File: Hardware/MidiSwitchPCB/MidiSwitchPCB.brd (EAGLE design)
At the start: 160 x 100 mm, 65 parts, among them IC1 74AHC1G04DBV, IC2 74AHC1G04DBV, K1 APF30212C, K2 APF30212C, K3 APF30212C, K4 APF30212C, K5 APF30212C, K6 APF30212C, K7 APF30212C, K8 APF30212C, Q1 BSS123, Q2 BSS123, Q3 BSS123, Q4 BSS123, Q5 BSS123, Q6 BSS123, Q7 BSS123, Q8 BSS123, X1 1503_09, X2 1503_09, X3 1503_09, X4 1503_09

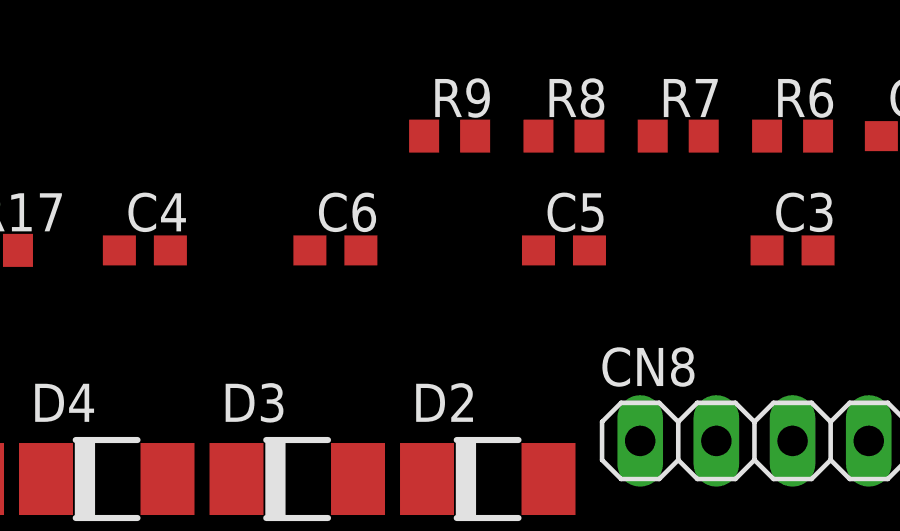
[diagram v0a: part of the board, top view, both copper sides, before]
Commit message: added switching capacitor to part list (changed cap-package in layout from 0603 to 1206)
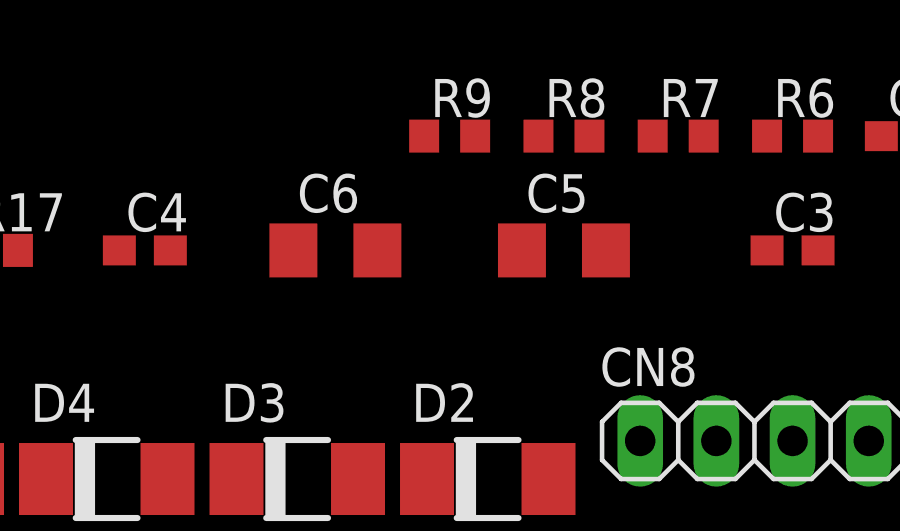
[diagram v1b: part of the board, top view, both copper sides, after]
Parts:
- C5, C6: device rcl:C0603 -> rcl:C1206
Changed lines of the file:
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@@
 <setting verticaltext="up"/>
 </settings>
-<grid distance="0.05" unitdist="inch" unit="inch" style="lines" multiple="1" display="no" altdistance="0.025" altunitdist="inch" altunit="inch"/>
+<grid distance="0.1" unitdist="mm" unit="mm" style="lines" multiple="1" display="yes" altdistance="0.025" altunitdist="inch" altunit="mm"/>
 <layers>
 <layer number="1" name="Top" color="4" fill="1" visible="yes" active="yes"/>
@@
 <element name="C3" library="rcl" package="C0603" value="100nF" x="-44.45" y="106.68"/>
 <element name="C4" library="rcl" package="C0603" value="22µF" x="-66.04" y="106.68"/>
-<element name="C5" library="rcl" package="C0603" value="100nF" x="-52.07" y="106.68"/>
-<element name="C6" library="rcl" package="C0603" value="100nF" x="-59.69" y="106.68"/>
+<element name="C5" library="rcl" package="C1206" value="100nF" x="-52.07" y="106.68"/>
+<element name="C6" library="rcl" package="C1206" value="100nF" x="-59.69" y="106.68"/>
 <element name="L1" library="rcl" package="POWER-CHOKE_WE-TPC" value="4.7µH" x="-80.01" y="35.56"/>
 <element name="C7" library="rcl" package="C0603" value="10µF 40V" x="-27.94" y="106.68"/>
@@
 <contactref element="C5" pad="1"/>
 <contactref element="L1" pad="2"/>
-<wire x1="-52.92" y1="106.68" x2="-19.922" y2="96.905" width="0" layer="19" extent="1-1"/>
-<wire x1="-80.01" y1="33.51" x2="-52.92" y2="106.68" width="0" layer="19" extent="1-1"/>
+<wire x1="-53.47" y1="106.68" x2="-19.922" y2="96.905" width="0" layer="19" extent="1-1"/>
+<wire x1="-80.01" y1="33.51" x2="-53.47" y2="106.68" width="0" layer="19" extent="1-1"/>
 </signal>
 <signal name="N$54">
 <contactref element="PS1" pad="19"/>
 <contactref element="C5" pad="2"/>
-<wire x1="-51.22" y1="106.68" x2="-19.922" y2="96.255" width="0" layer="19" extent="1-1"/>
+<wire x1="-50.67" y1="106.68" x2="-19.922" y2="96.255" width="0" layer="19" extent="1-1"/>
 </signal>
 <signal name="N$55">
@@
 <contactref element="PS1" pad="2"/>
 <contactref element="C6" pad="1"/>
-<wire x1="-60.54" y1="106.68" x2="-25.798" y2="96.255" width="0" layer="19" extent="1-1"/>
-<wire x1="-80.01" y1="37.61" x2="-60.54" y2="106.68" width="0" layer="19" extent="1-1"/>
+<wire x1="-61.09" y1="106.68" x2="-25.798" y2="96.255" width="0" layer="19" extent="1-1"/>
+<wire x1="-80.01" y1="37.61" x2="-61.09" y2="106.68" width="0" layer="19" extent="1-1"/>
 </signal>
 <signal name="N$56">
 <contactref element="C6" pad="2"/>
 <contactref element="PS1" pad="3"/>
-<wire x1="-58.84" y1="106.68" x2="-25.798" y2="95.605" width="0" layer="19" extent="1-1"/>
+<wire x1="-58.29" y1="106.68" x2="-25.798" y2="95.605" width="0" layer="19" extent="1-1"/>
 </signal>
 <signal name="N$53">

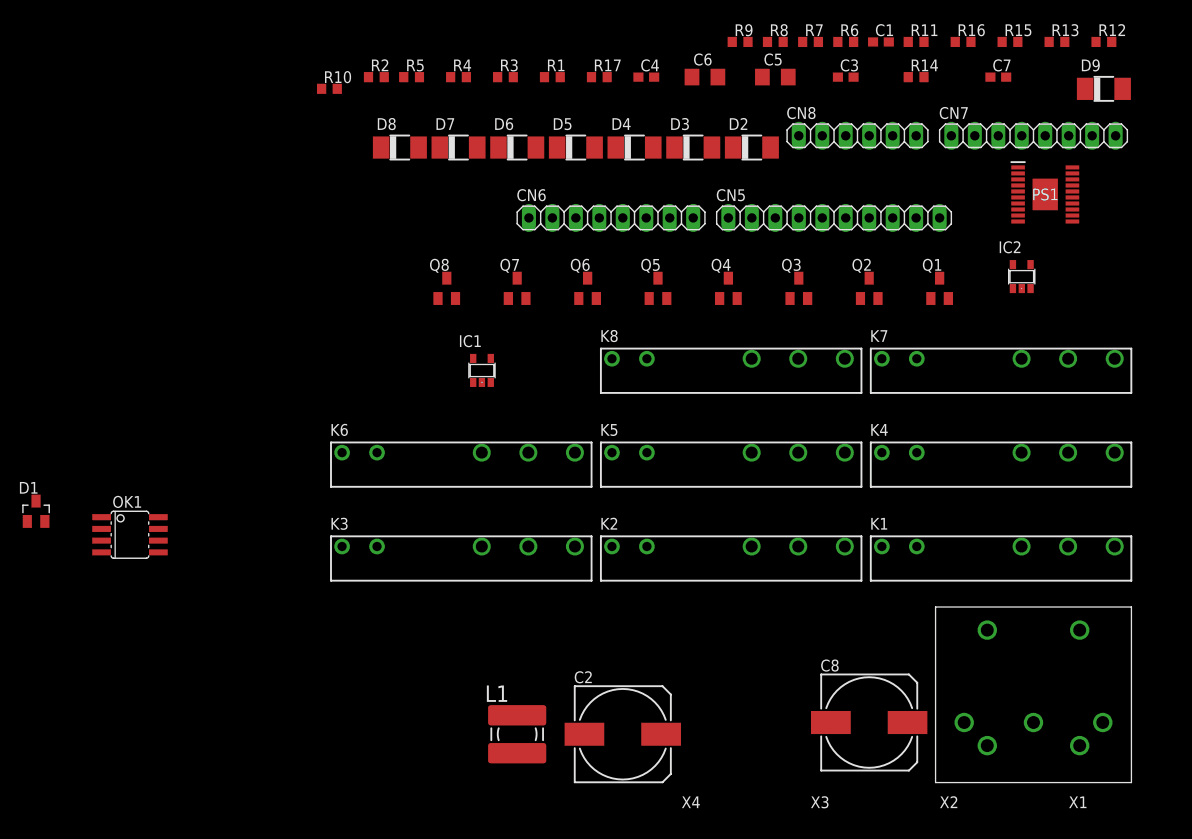
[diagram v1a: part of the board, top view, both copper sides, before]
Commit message: added some part libraries
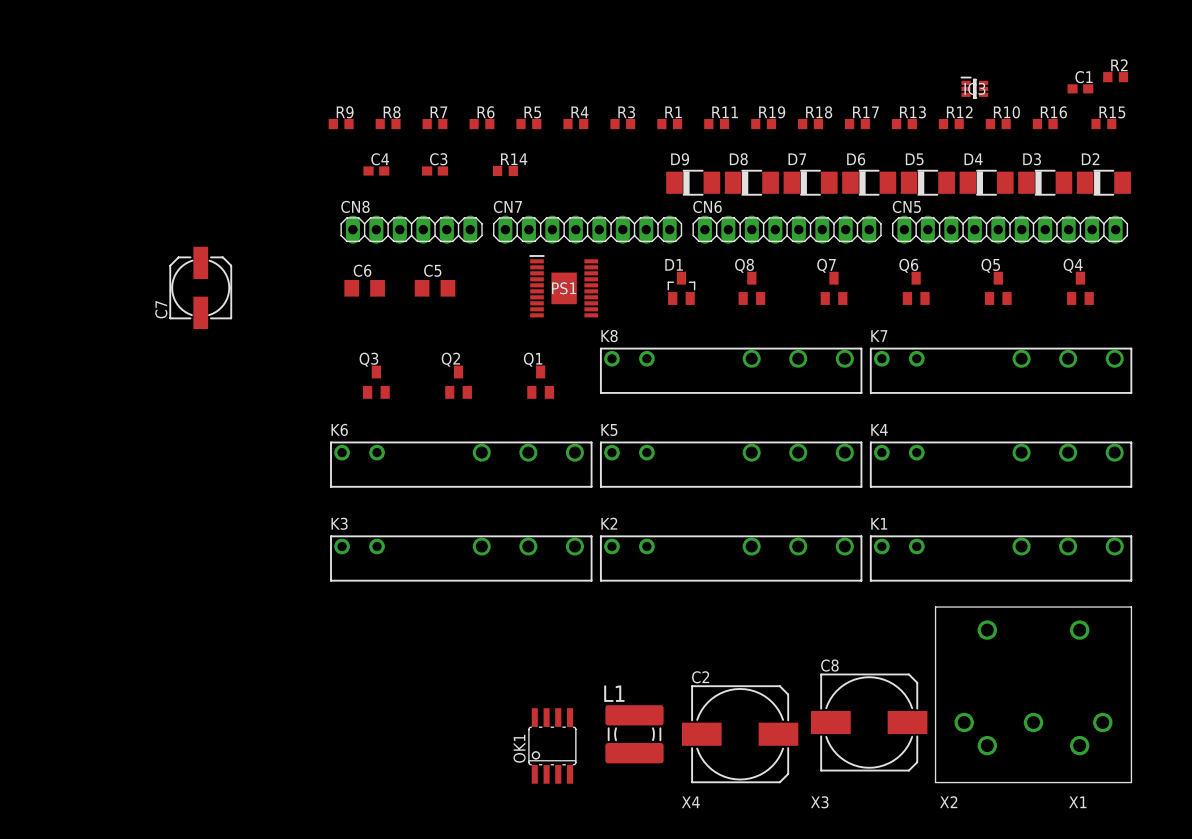
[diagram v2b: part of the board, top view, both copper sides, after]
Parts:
- removed IC1, IC2: 74AHC1G04DBV, 74xx-little-de:SOT23-5
- added IC3: 74LVC2G04GW,125, 74LVC2G04GW_125:SOT65P210X110-6N
- added R18, R19: 0R, rcl:R0603
- C7: device rcl:C0603 -> rcl:153CLV-0605
- moved C7 89.3 mm to (-114.3, 83.9), turned to 90 degrees
- moved R2 80.0 mm to (-15.2, 106.7)
- moved D1 73.9 mm to (-62.2, 83.8)
- moved R10 72.5 mm to (-27.9, 101.6)
- moved PS1 53.1 mm to (-74.9, 83.8)
- moved OK1 51.1 mm to (-76.2, 34.3), turned to 0 degrees
- moved CN7 49.3 mm to (-72.4, 90.2)
- moved CN8 49.3 mm to (-91.4, 90.2)
- moved Q3 46.8 mm to (-95.2, 73.7)
- moved C3 45.6 mm to (-88.9, 96.5)
- moved D9 45.6 mm to (-61.0, 95.2)
- moved Q2 45.6 mm to (-86.4, 73.7)
- moved R14 45.6 mm to (-81.3, 96.5)
- moved Q1 44.4 mm to (-77.5, 73.7)
- moved R9 44.1 mm to (-99.1, 101.6)
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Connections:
- new net N$58: PS1.8, R18.2, R19.1
- new net VCC_3_3: IC3.5, OK1.8, R3.2, R5.2
- new net VCC_6-8: C1.1, C2.+, C3.1, C4.1, CN6.8, D2.C, D3.C, D4.C, D5.C, D6.C, D7.C, D8.C, D9.C, K1.1, K2.1, K3.1, K4.1, K5.1, K6.1, K7.1, K8.1, PS1.16, PS1.17, R14.1, R15.2
- net GND: now also C7.-, IC3.2, R19.2; no longer C7.2, IC1.3, IC2.3
- net MIDI_RX: now also IC3.3; no longer IC1.2
- net N$1: now also IC3.1, IC3.4; no longer IC1.4, IC2.2
- net N$11: now also IC3.6; no longer IC2.4
- net N$53: now also C7.+, R18.1; no longer C7.1
- net VCC: now also CN6.4; no longer C1.1, C2.+, C3.1, C4.1, CN6.8, D2.C, D3.C, D4.C, D5.C, D6.C, D7.C, D8.C, D9.C, IC1.5, IC2.5, K1.1, K2.1, K3.1, K4.1, K5.1, K6.1, K7.1, K8.1, OK1.8, PS1.16, PS1.17, R14.1, R15.2, R3.2, R5.2

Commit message: continued searching parts
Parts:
- added R20, R21, R22, R23, R24, R25, R26, R27: (no value), rcl:R0603
- C4: device rcl:C0603 -> rcl:C1206
- C8: device rcl:153CLV-1012 -> rcl:C0805
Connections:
- new net N$59: K1.1, R20.1
- new net N$60: K2.1, R22.1
- new net N$61: K3.1, R21.1
- new net N$62: K4.1, R23.1
- new net N$63: K5.1, R24.1
- new net N$64: K6.1, R25.1
- new net N$65: K7.1, R26.1
- new net N$66: K8.1, R27.1
- net GND: now also C8.2; no longer C8.-
- net N$57: now also C8.1; no longer C8.+
- net VCC_6-8: now also R20.2, R21.2, R22.2, R23.2, R24.2, R25.2, R26.2, R27.2; no longer K1.1, K2.1, K3.1, K4.1, K5.1, K6.1, K7.1, K8.1

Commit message: changed some device packages
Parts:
- removed K1: APF30212C, relay:APF30212C
- added J1: 694108106102, SamacSys_Parts:694108106102
- added U$3: G6L-1F-TR_DC5-NEW, SamacSys_Parts:G6L1FTRDC5
- moved U$1 221.4 mm to (127.0, 86.0)
- moved CN8 214.6 mm to (122.2, 70.0)
- moved CN7 203.8 mm to (119.7, 22.0)
- moved OK1 190.6 mm to (113.8, 49.3)
- moved C7 181.0 mm to (55.7, 21.9)
- moved PS1 169.3 mm to (89.1, 41.8)
- moved CN6 154.1 mm to (102.0, 70.0)
- moved R20 143.6 mm to (16.9, 46.7)
- moved R21 143.6 mm to (16.9, 43.3)
- moved R22 143.6 mm to (16.9, 40.0)
- moved R23 143.6 mm to (16.9, 36.6)
- moved R24 143.6 mm to (16.9, 33.3)
- moved R25 143.6 mm to (16.9, 29.9)
- moved R26 143.6 mm to (16.9, 26.6)
- moved R27 143.6 mm to (16.9, 23.2)
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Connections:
- removed net N$53: C7.+, PS1.4, PS1.5, PS1.6, R18.1
- new net N$67: C7.+, J1.1, PS1.4, PS1.5, PS1.6, R18.1
- net GND: now also J1.3
- net N$12: now also U$3.8; no longer K1.2
- net N$36: now also U$3.4; no longer K1.NO
- net N$38: now also U$3.2; no longer K1.COM, K1.NC
- net N$59: now also U$3.5; no longer K1.1

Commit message: placed devices on the layout
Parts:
- removed C3: 100nF, rcl:C0603
- removed C4: 22µF, rcl:C1206
- removed C5, C6: 100nF, rcl:C1206
- removed C7: 10µF 40V, rcl:153CLV-0605
- removed C8: 4.7 µF, rcl:C0805
- removed K2, K3, K4, K5, K6, K7, K8: APF30212C, relay:APF30212C
- removed R14: 10-100k, rcl:R0603
- removed R17, R18, R19: 0R, rcl:R0603
- added C_BST1, C_BST2: 100nF, rcl:C1206
- added C_IN: 10µF 40V, rcl:153CLV-0605
- added C_OUT: 22µF, rcl:C1206
- added C_REG: 4.7 µF, rcl:C0805
- added C_SENS: 100nF, rcl:C0603
- added R_DLY, R_PWRL_DOWN, R_PWRL_UP: 0R, rcl:R0603
- added R_PG: 10-100k, rcl:R0603
- added U$10, U$4, U$5, U$6, U$7, U$8, U$9: G6L-1F-TR_DC5-NEW, SamacSys_Parts:G6L1FTRDC5
- L1: device rcl:POWER-CHOKE_WE-TPC -> NRS8030T4R7MJGJ:NRS8030T4R7MJGJ
- moved R4 202.8 mm to (122.4, 49.9), turned to 90 degrees
- moved R5 202.1 mm to (116.0, 47.8), turned to 180 degrees
- moved R3 199.7 mm to (122.0, 42.0), turned to 90 degrees
- moved R1 190.9 mm to (113.7, 30.7)
- moved D1 187.6 mm to (117.7, 30.8), turned to 90 degrees
- moved C1 175.1 mm to (140.2, 32.4)
- moved R6 173.4 mm to (85.0, 62.0), turned to 180 degrees
- moved R8 168.4 mm to (64.0, 43.1), turned to 180 degrees
- moved R16 166.1 mm to (135.4, 51.0), turned to 90 degrees
- moved R15 163.0 mm to (139.1, 53.1)
- moved IC3 159.9 mm to (119.5, 50.0), turned to 270 degrees
- moved Q1 158.9 mm to (81.0, 63.0), turned to 90 degrees
- moved Q3 158.0 mm to (59.9, 44.0), turned to 90 degrees
- moved R7 157.9 mm to (64.0, 62.0), turned to 180 degrees
- moved R9 147.4 mm to (43.0, 62.1), turned to 180 degrees
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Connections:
- removed net N$50: R15.1
- removed net N$66: K8.1, R27.1
- new net N$53: R23.1, U$6.5
- net GND: now also C_IN.-, C_OUT.2, C_REG.2, C_SENS.2, R_DLY.2, R_PWRL_DOWN.2; no longer C3.2, C4.2, C7.-, C8.2, R17.2, R19.2
- net N$13: now also U$5.8; no longer K3.2
- net N$16: now also U$6.8; no longer K4.2
- net N$19: now also U$5.4; no longer K3.NO
- net N$20: now also U$4.8; no longer K2.2
- net N$22: now also U$6.4; no longer K4.NO
- net N$23: now also U$5.2, U$6.2; no longer K3.COM, K3.NC, K4.COM, K4.NC
- net N$24: now also U$7.8; no longer K5.2
- net N$26: now also U$8.8; no longer K6.2
- net N$29: now also U$7.4; no longer K5.NO
- net N$30: now also U$8.4; no longer K6.NO
- net N$32: now also U$7.2, U$8.2; no longer K5.COM, K5.NC, K6.COM, K6.NC
- net N$33: now also U$9.8; no longer K7.2
- net N$35: now also U$10.8; no longer K8.2
- net N$37: now also U$4.4; no longer K2.NO
- net N$38: now also U$4.2; no longer K2.COM, K2.NC
- net N$41: now also U$9.4; no longer K7.NO
- net N$42: now also U$10.4; no longer K8.NO
- net N$43: now also U$10.2, U$9.2; no longer K7.COM, K7.NC, K8.COM, K8.NC
- net N$48: now also R_DLY.1; no longer R17.1
- net N$49: now also R15.1
- net N$51: now also C_BST2.1; no longer C5.1
- net N$52: now also R_PG.2; no longer R14.2
- net N$54: now also C_BST2.2; no longer C5.2
- net N$55: now also C_BST1.1; no longer C6.1
- net N$56: now also C_BST1.2; no longer C6.2
- net N$57: now also C_REG.1; no longer C8.1
- net N$58: now also R_PWRL_DOWN.1, R_PWRL_UP.2; no longer R18.2, R19.1
- net N$60: now also U$4.5; no longer K2.1
- net N$61: now also U$5.5; no longer K3.1
- net N$62: now also R27.1, U$10.5; no longer K4.1, R23.1
- net N$63: now also U$7.5; no longer K5.1
- net N$64: now also U$8.5; no longer K6.1
- net N$65: now also U$9.5; no longer K7.1
- net N$67: now also C_IN.+, R_PWRL_UP.1; no longer C7.+, R18.1
- net VCC_6-8: now also C_OUT.1, C_SENS.1, R_PG.1; no longer C3.1, C4.1, R14.1

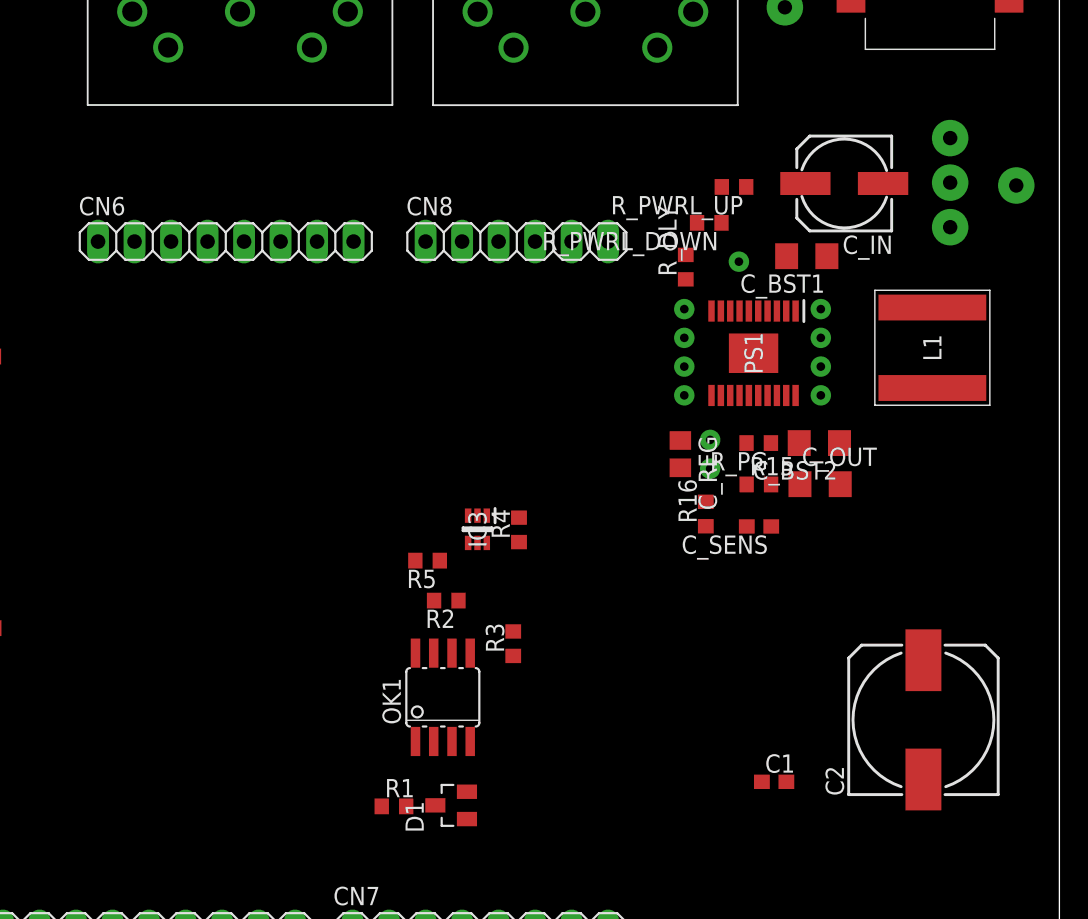
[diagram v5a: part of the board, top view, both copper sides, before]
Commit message: Finished device placement and added a fuse as well as an ESD diode
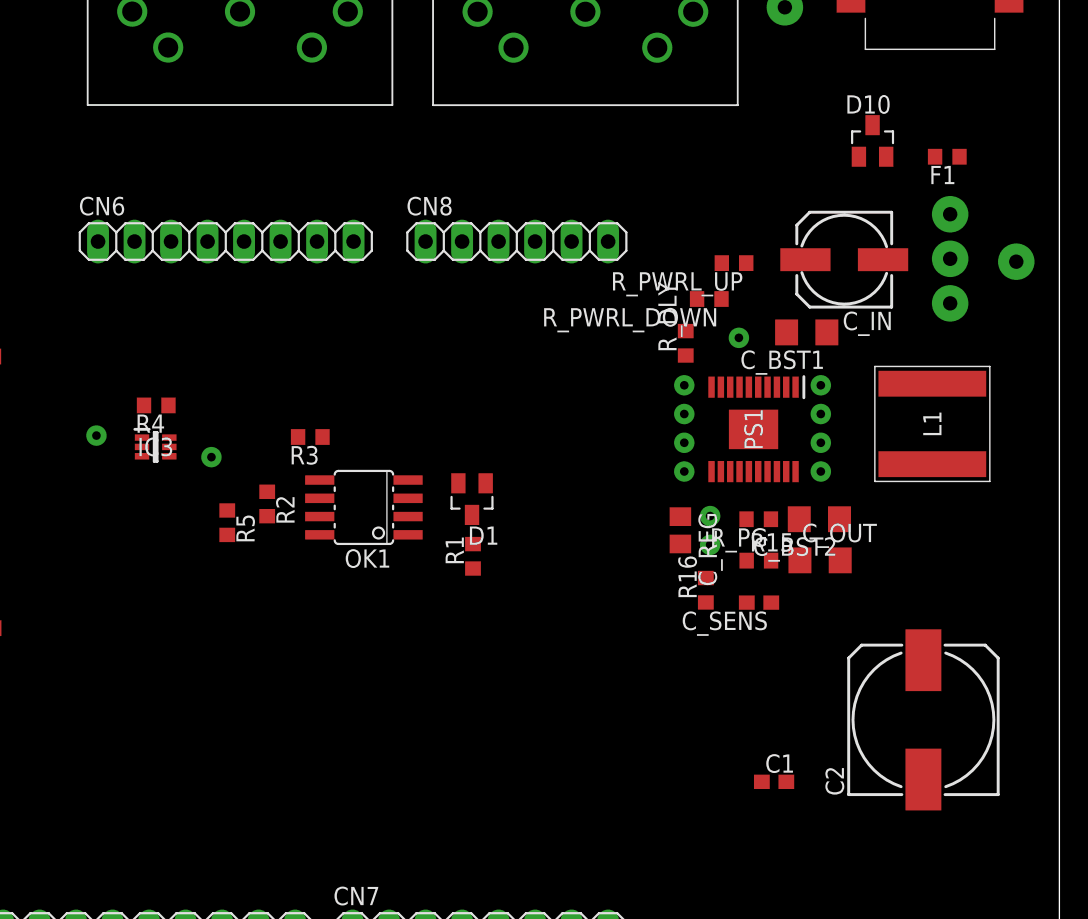
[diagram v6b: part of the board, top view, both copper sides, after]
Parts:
- added D10: BAS70-06, diode:SOT23
- added F1: 1A, rcl:R0603
- moved R4 26.7 mm to (97.2, 58.6), turned to 180 degrees
- moved IC3 23.1 mm to (97.1, 55.7), turned to 0 degrees
- moved D1 21.4 mm to (119.1, 52.1), turned to 180 degrees
- moved R3 20.2 mm to (107.9, 56.4), turned to 180 degrees
- moved R1 18.2 mm to (119.2, 48.1), turned to 90 degrees
- moved OK1 14.3 mm to (111.6, 51.5), turned to 90 degrees
- moved R5 14.2 mm to (102.1, 50.4), turned to 270 degrees
- moved R2 14.2 mm to (104.9, 51.7), turned to 270 degrees
- moved C_IN 5.30 mm to (145.0, 68.7)
- moved C_BST1 5.30 mm to (142.4, 63.7)
- moved C_REG 5.30 mm to (133.6, 49.9)
- moved R15 5.30 mm to (139.1, 47.8)
- moved C_BST2 5.30 mm to (143.3, 50.7)
- moved C_OUT 5.30 mm to (143.3, 47.8)
- moved C_SENS 5.30 mm to (139.1, 44.9)
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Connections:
- new net N$50: F1.1, J1.1
- net GND: now also D10.1
- net N$67: now also D10.2, F1.2; no longer J1.1
- net VCC: now also C1.1, C2.+, CN6.8
- net VCC_6-8: no longer C1.1, C2.+, CN6.8

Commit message: started routing
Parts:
- moved C1 10.3 mm to (144.0, 41.9)
- moved R3 9.91 mm to (109.4, 46.6)
- moved C2 3.52 mm to (147.4, 35.1), turned to 180 degrees
- moved C_OUT 3.31 mm to (144.8, 44.8)
- moved C_BST2 1.55 mm to (144.5, 49.8), turned to 270 degrees
- moved C_REG 0.71 mm to (132.9, 49.9)
- moved R_PWRL_UP 0.20 mm to (137.3, 68.7)
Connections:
- net N$50 renamed VIN
- net N$67 renamed VIN_FUSED
- removed net VCC: C1.1, C2.+, CN6.4, CN6.8
- net VCC_3_3: now also CN6.4
- net VCC_6-8: now also C1.1, C2.+, CN6.8
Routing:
- net N$5: track 0.00 -> 55.8 mm
- net N$8: track 0.00 -> 53.4 mm
- net N$3: track 0.00 -> 46.1 mm
- net VCC_3_3: track 0.00 -> 39.0 mm, vias 0 -> 2
- net N$9: track 0.00 -> 34.4 mm
- net VIN_FUSED: track 0.00 -> 31.2 mm
- net GND: track 0.00 -> 24.0 mm, vias 18 -> 19
- net VIN: track 0.00 -> 20.1 mm
- net N$55: track 0.00 -> 16.1 mm
- net MIDI_RX: track 0.00 -> 15.5 mm
- net N$51: track 0.00 -> 14.4 mm
- net N$1: track 0.00 -> 14.0 mm
- net N$49: track 0.00 -> 10.3 mm
- net N$58: track 0.00 -> 10.1 mm
- net N$54: track 0.00 -> 7.99 mm
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- added copper zone on layer 1, net GND
- added copper zone on layer 16, net GND
- added copper zone on layer 1, net VCC_6-8
